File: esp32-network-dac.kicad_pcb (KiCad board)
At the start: 6 copper layers, 46 parts, among them J1 USB4510-03-1-A, J2 SJ1-3533NS, J3 Conn_01x04_Male, U1 PCM5122PW, U2 ESP32-WROVER-EM213EH2864PH3Q0, U3 MCP1825S, U4 MCP1825S

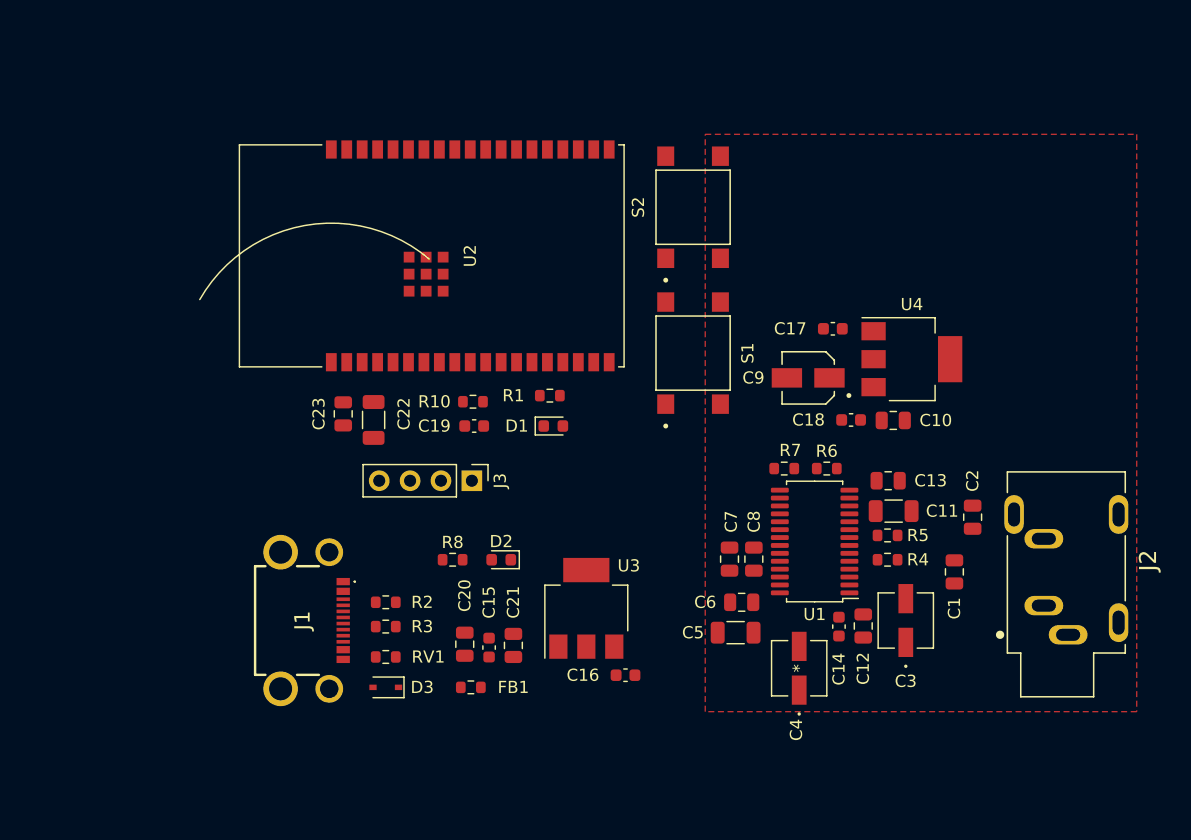
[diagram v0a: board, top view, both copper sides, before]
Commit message: Updates to PCB - traces all done and most ground planes etc.
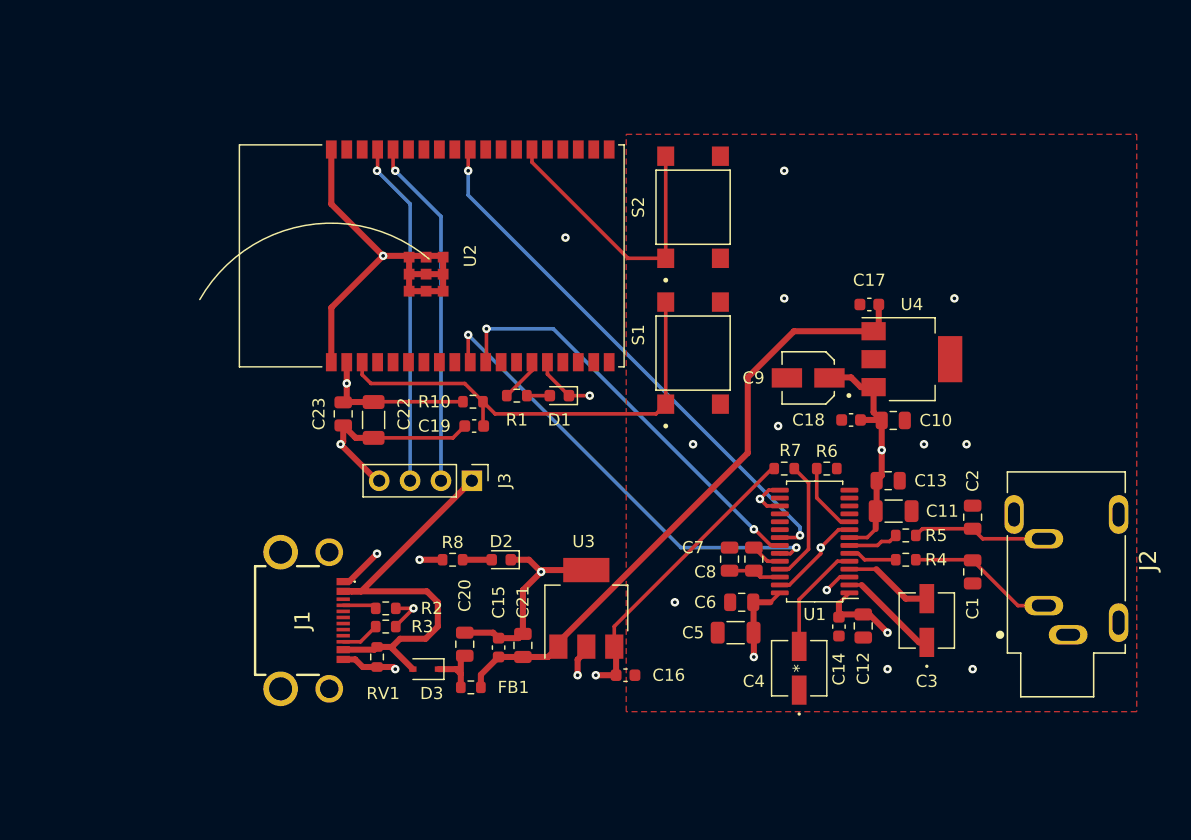
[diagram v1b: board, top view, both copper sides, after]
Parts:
- moved D3 3.61 mm to (109.5, 117.5)
- moved C17 3.61 mm to (146.0, 87.5)
- moved R1 2.72 mm to (117.0, 95.0)
- moved D1 2.55 mm to (120.5, 95.0), turned to 180 degrees
- moved C3 1.73 mm to (150.7, 113.5)
- moved C1 1.50 mm to (154.5, 109.5)
- moved R4 1.50 mm to (149.0, 108.5)
- moved R5 1.50 mm to (149.0, 106.5)
- moved C15 0.78 mm to (115.5, 115.7)
- moved C21 0.78 mm to (117.5, 115.5)
- moved RV1 0.72 mm to (105.5, 116.5), turned to -90 degrees
- moved R2 0.50 mm to (106.2, 112.5)
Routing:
- net GND: track 0.06 -> 108.0 mm, vias 0 -> 22
- net VBUS_FILT: track 0.00 -> 51.3 mm
- net +3V3: track 0.00 -> 46.5 mm, vias 0 -> 4
- net PCM_BCK: track 0.00 -> 44.9 mm, vias 0 -> 2
- net PCM_LRCK: track 0.00 -> 38.1 mm, vias 0 -> 2
- net RESET: track 0.00 -> 38.1 mm
- net VBUS: track 0.00 -> 34.9 mm
- net PCM_DIN: track 0.00 -> 34.3 mm, vias 0 -> 2
- net ESP32_Rx: track 0.00 -> 28.9 mm, vias 0 -> 1
- net ESP32_Tx: track 0.00 -> 28.4 mm, vias 0 -> 1
- net +3.3VA: track 0.00 -> 27.4 mm, vias 0 -> 2
- net GPIO0: track 0.00 -> 23.7 mm
- net /JACKL: track 0.00 -> 12.1 mm
- net /JACKR: track 0.00 -> 11.1 mm
- net /XSMT: track 0.00 -> 10.2 mm
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- added copper zone on In3.Cu, net +3.3VA
- added copper zone on In3.Cu, net +3V3
- added copper zone on In1.Cu, net GND
- added copper zone on In3.Cu, net GND

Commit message: Changed footrpints to remove DRC warnings. Added board outline.
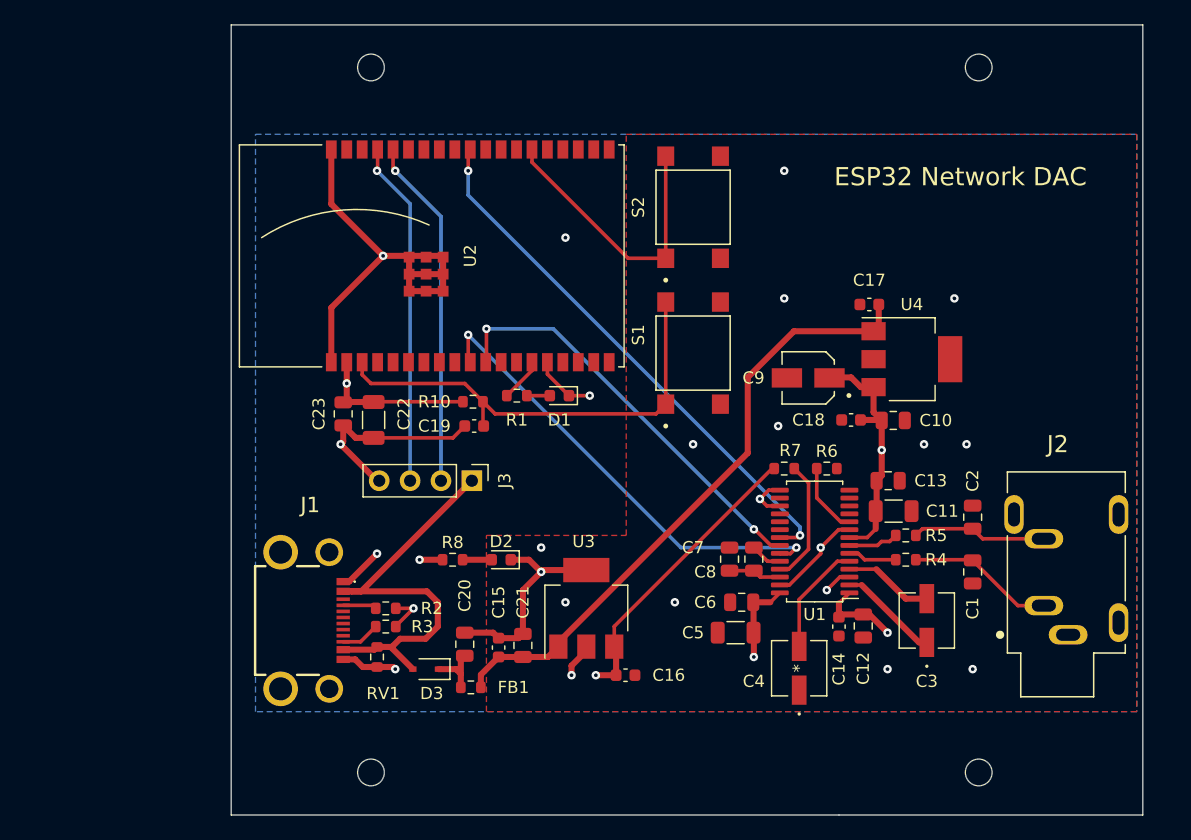
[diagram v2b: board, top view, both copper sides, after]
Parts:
- added H1: MountingHole, MountingHole:MountingHole_2.2mm_M2, F.Cu at (105.0, 126.0)
- added H2: MountingHole, MountingHole:MountingHole_2.2mm_M2, F.Cu at (105.0, 68.0)
- added H3: MountingHole, MountingHole:MountingHole_2.2mm_M2, F.Cu at (155.0, 68.0)
- added H4: MountingHole, MountingHole:MountingHole_2.2mm_M2, F.Cu at (155.0, 126.0)
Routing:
- net GND: track 108.0 -> 108.2 mm, vias 22 -> 24
- added copper zone on B.Cu, net GND
- added copper zone on In4.Cu, net GND
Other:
- board outline added: 75 x 65 mm
- board text added: "ESP32 Network DAC"

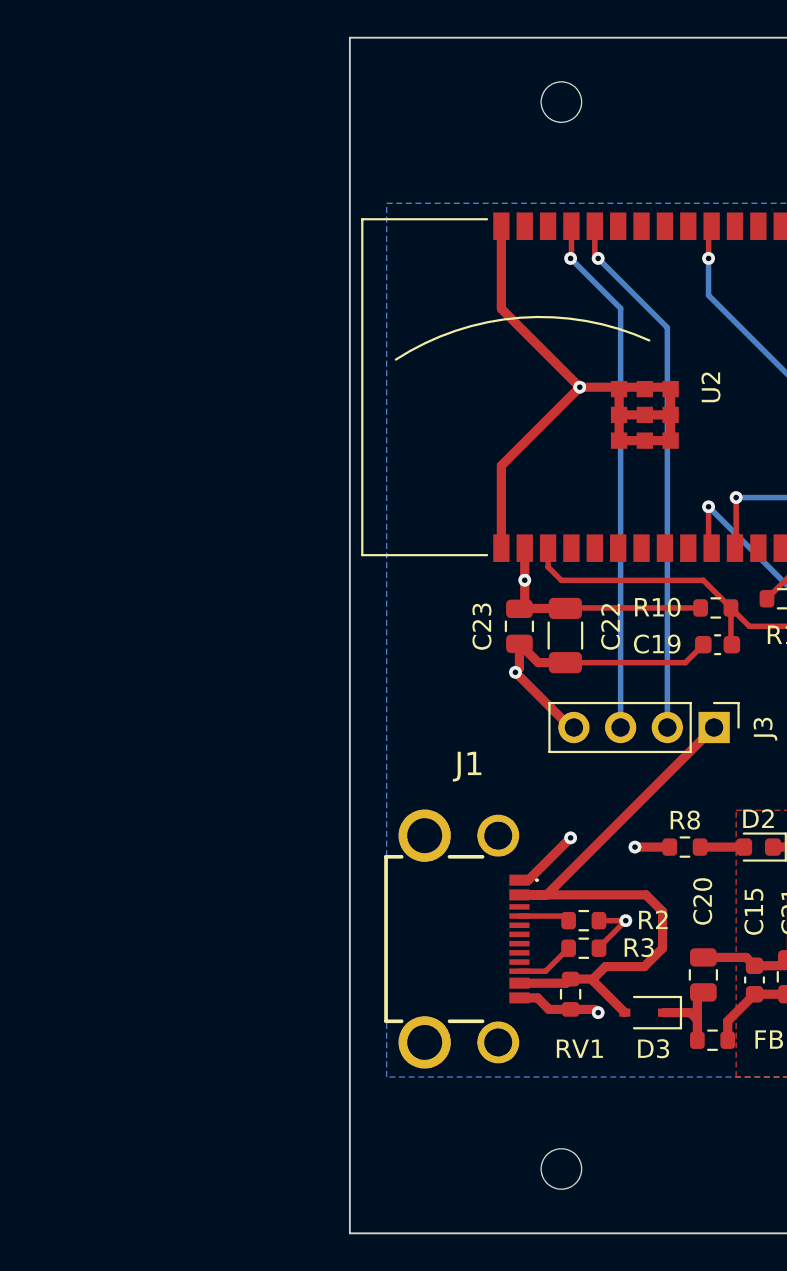
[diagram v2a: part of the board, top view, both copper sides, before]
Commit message: Updates to USB C receptive - replaced mid-mount recepticle with SMT
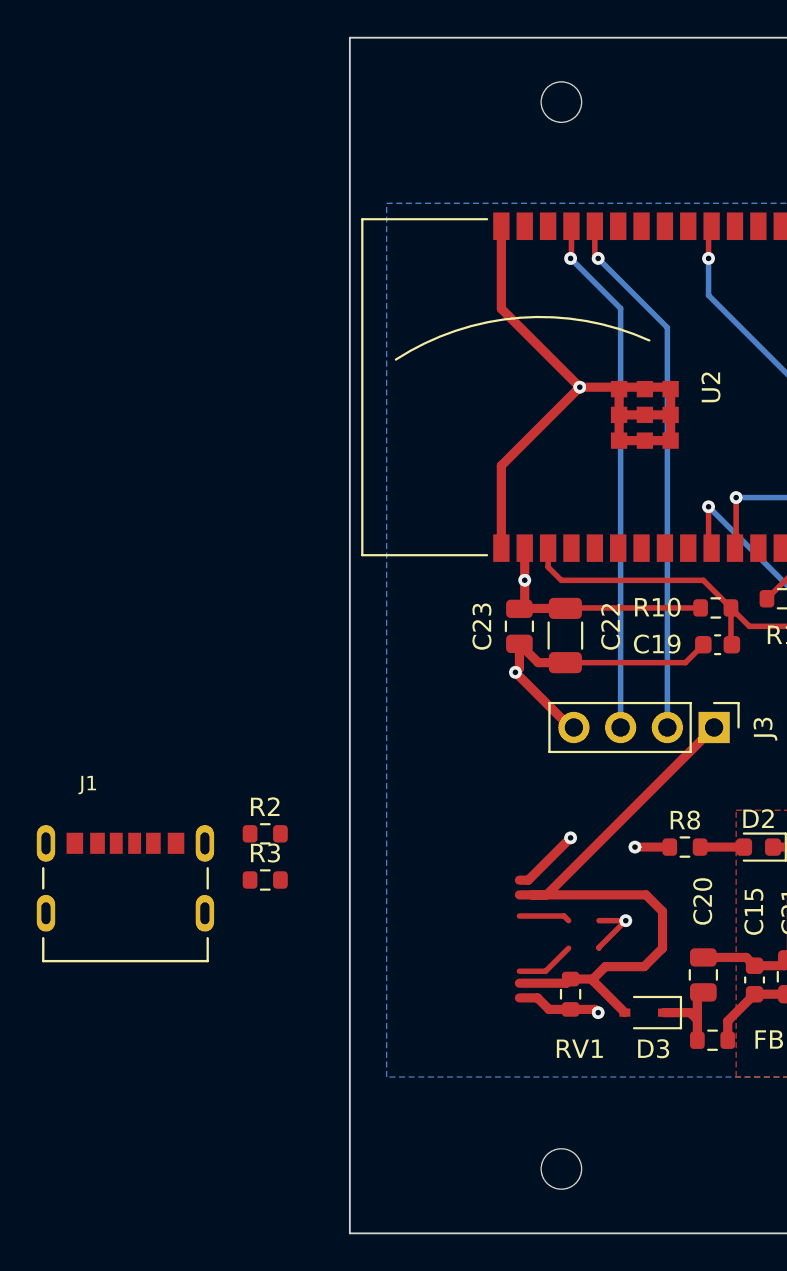
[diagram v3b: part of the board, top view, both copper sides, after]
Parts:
- J1: value USB4510-03-1-A -> UJC-HP-3-SMT-TR; footprint library:USB4510031A -> library:CUI_UJC-HP-3-SMT-TR
- moved J1 18.2 mm to (81.3, 108.3), turned to 0 degrees
- moved R2 17.9 mm to (88.9, 107.8)
- moved R3 17.7 mm to (88.9, 110.3)
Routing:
- added copper zone on In2.Cu, net +3.3VA
- added copper zone on In2.Cu, net +3V3
- added copper zone on In2.Cu, net GND
- removed copper zone on In3.Cu, net +3.3VA
- removed copper zone on In3.Cu, net +3V3
- removed copper zone on In3.Cu, net GND
- removed copper zone on In4.Cu, net GND
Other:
- copper layers 6 -> 4

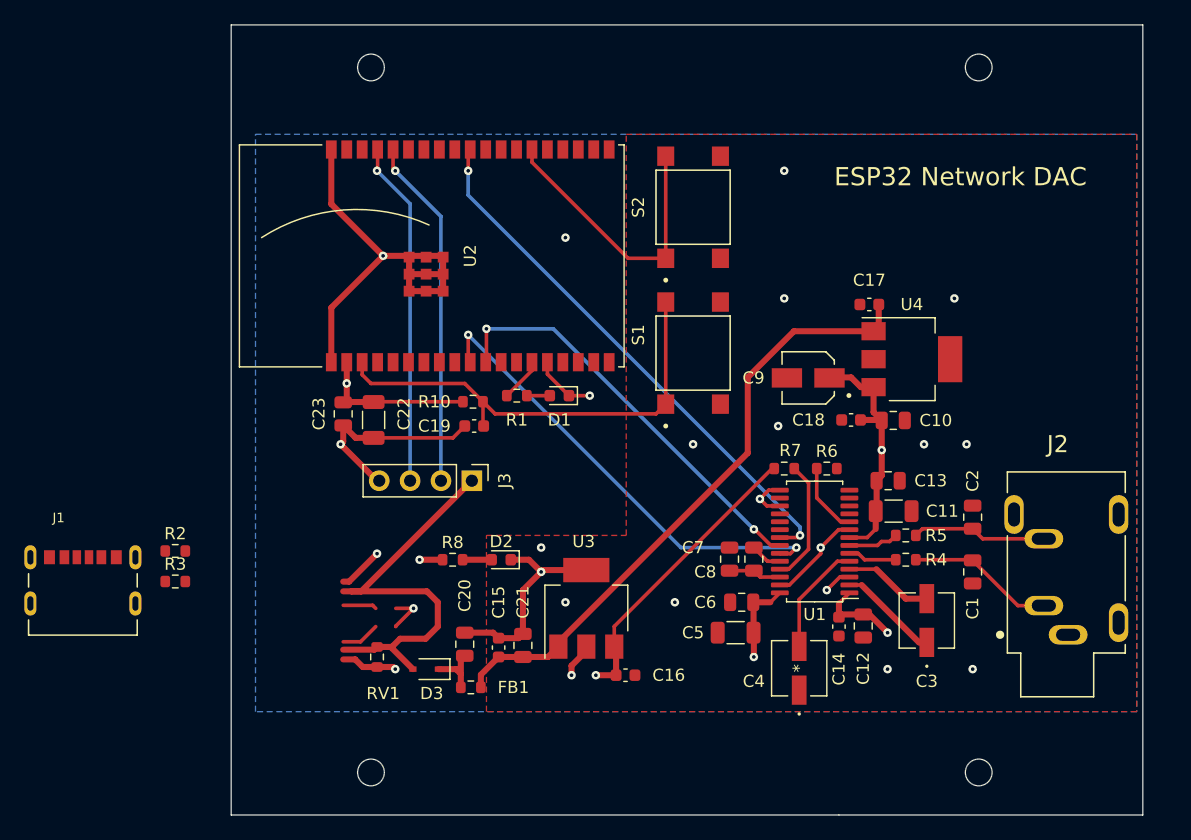
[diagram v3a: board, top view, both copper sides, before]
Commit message: Finalised v0.1 design and created manufacturing files
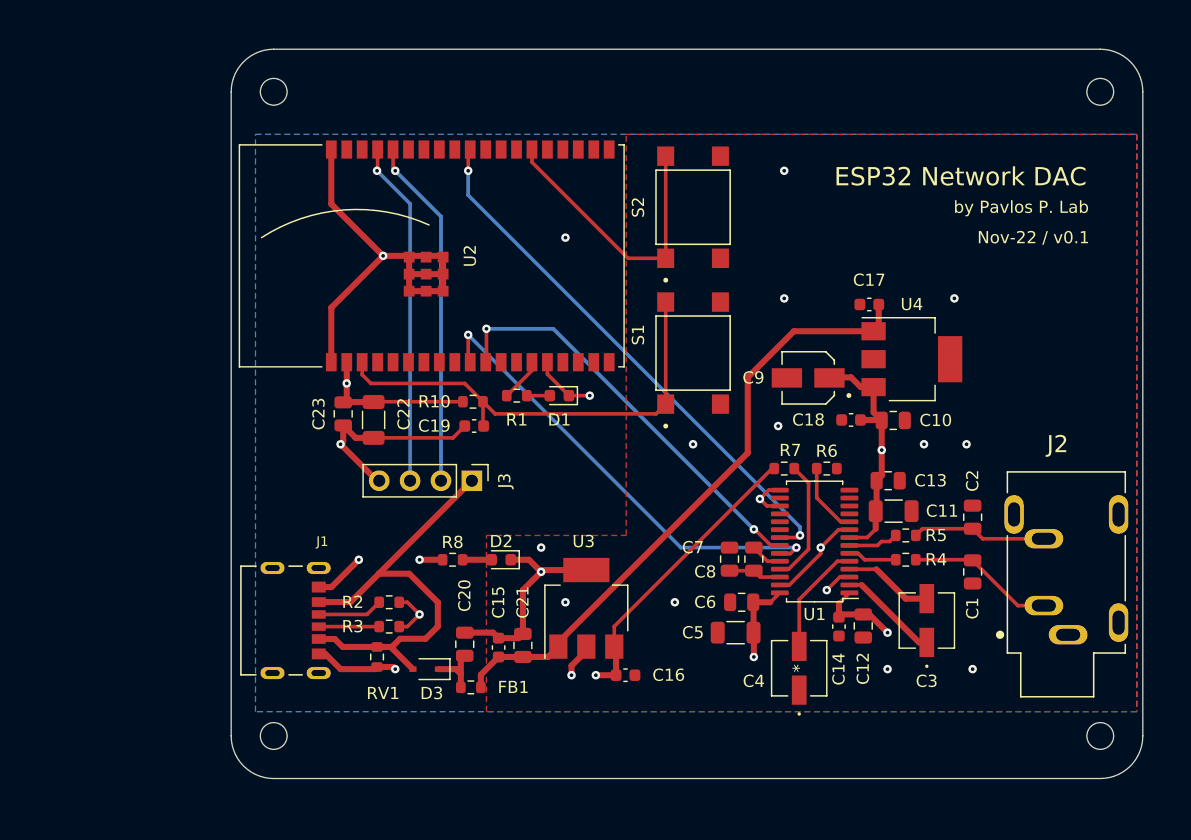
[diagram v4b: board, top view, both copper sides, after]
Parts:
- moved J1 20.1 mm to (100.7, 113.5), turned to -90 degrees
- moved R2 18.1 mm to (106.5, 112.0), turned to 180 degrees
- moved R3 18.0 mm to (106.5, 114.0), turned to 180 degrees
- moved H4 10.4 mm to (165.0, 123.0)
- moved H3 10.2 mm to (165.0, 70.0)
- moved H1 8.54 mm to (97.0, 123.0)
- moved H2 8.25 mm to (97.0, 70.0)
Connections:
- R2 pad 1: /CC1 -> GND
- R2 pad 2: GND -> /CC1
- R3 pad 1: /CC2 -> GND
- R3 pad 2: GND -> /CC2
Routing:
- net GND: track 108.2 -> 111.7 mm
- net VBUS: track 34.9 -> 37.9 mm
- net /CC1: track 2.78 -> 5.38 mm
- net /CC2: track 3.19 -> 4.97 mm
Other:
- board size 75 x 65 mm -> 75 x 60 mm
- board text added: "JLCJLCJLCJLC"
- board text added: "Nov-22 / v0.1"
- board text added: "by Pavlos P. Lab"
